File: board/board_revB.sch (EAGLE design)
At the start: 78 parts, among them Q1 ULN2003AS, Q2 ULN2003AD, Y1 8Mhz

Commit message: [Board] Fix files
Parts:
- removed IC_REF: MC1525TT, microchip:MC1525TT
- added IC_EE: 25LC040ST, microchip:25LC040ST
- added TP2: (no value), microbuilder:TESTPOINTROUND1MM
- renumbered IC_REG1 to IC_REG
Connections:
- removed net VAN: C30.1, C31.1, IC_REF.VO, STM32AN_POWER.VDDA
- new net SPI2_MISO: IC_EE.SO, STM32PORTB_H.PB14
- new net SPI2_MOSI: IC_EE.SI, STM32PORTB_H.PB15
- new net SPI2_NSS: IC_EE.!CS, STM32PORTB_H.PB12
- new net SPI2_SCK: IC_EE.SCK, STM32PORTB_H.PB13
- net +3V3: now also C30.1, C31.1, IC_EE.!WP, IC_EE.VCC, STM32AN_POWER.VDDA, TP2.P$1; no longer IC_REF.VIN
- net GND: now also IC_EE.GND; no longer IC_REF.GND
- net USB_CTRL: now also STM32PORTC_H.PC8; no longer STM32PORTB_H.PB13

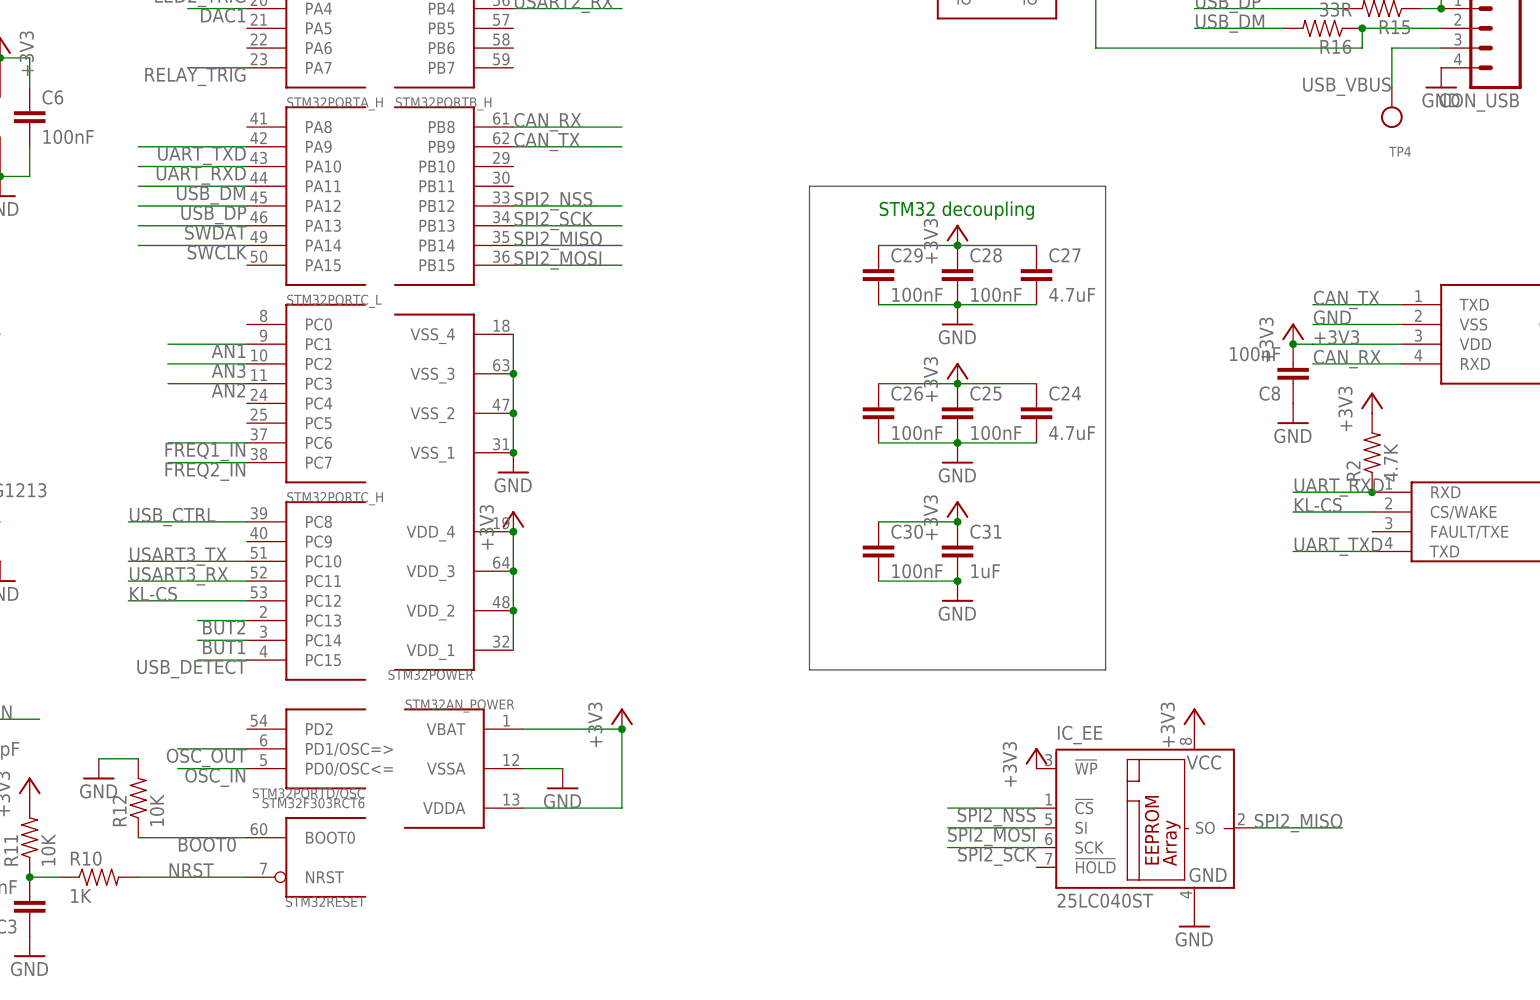
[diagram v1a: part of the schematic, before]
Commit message: [Board] Layout improvements
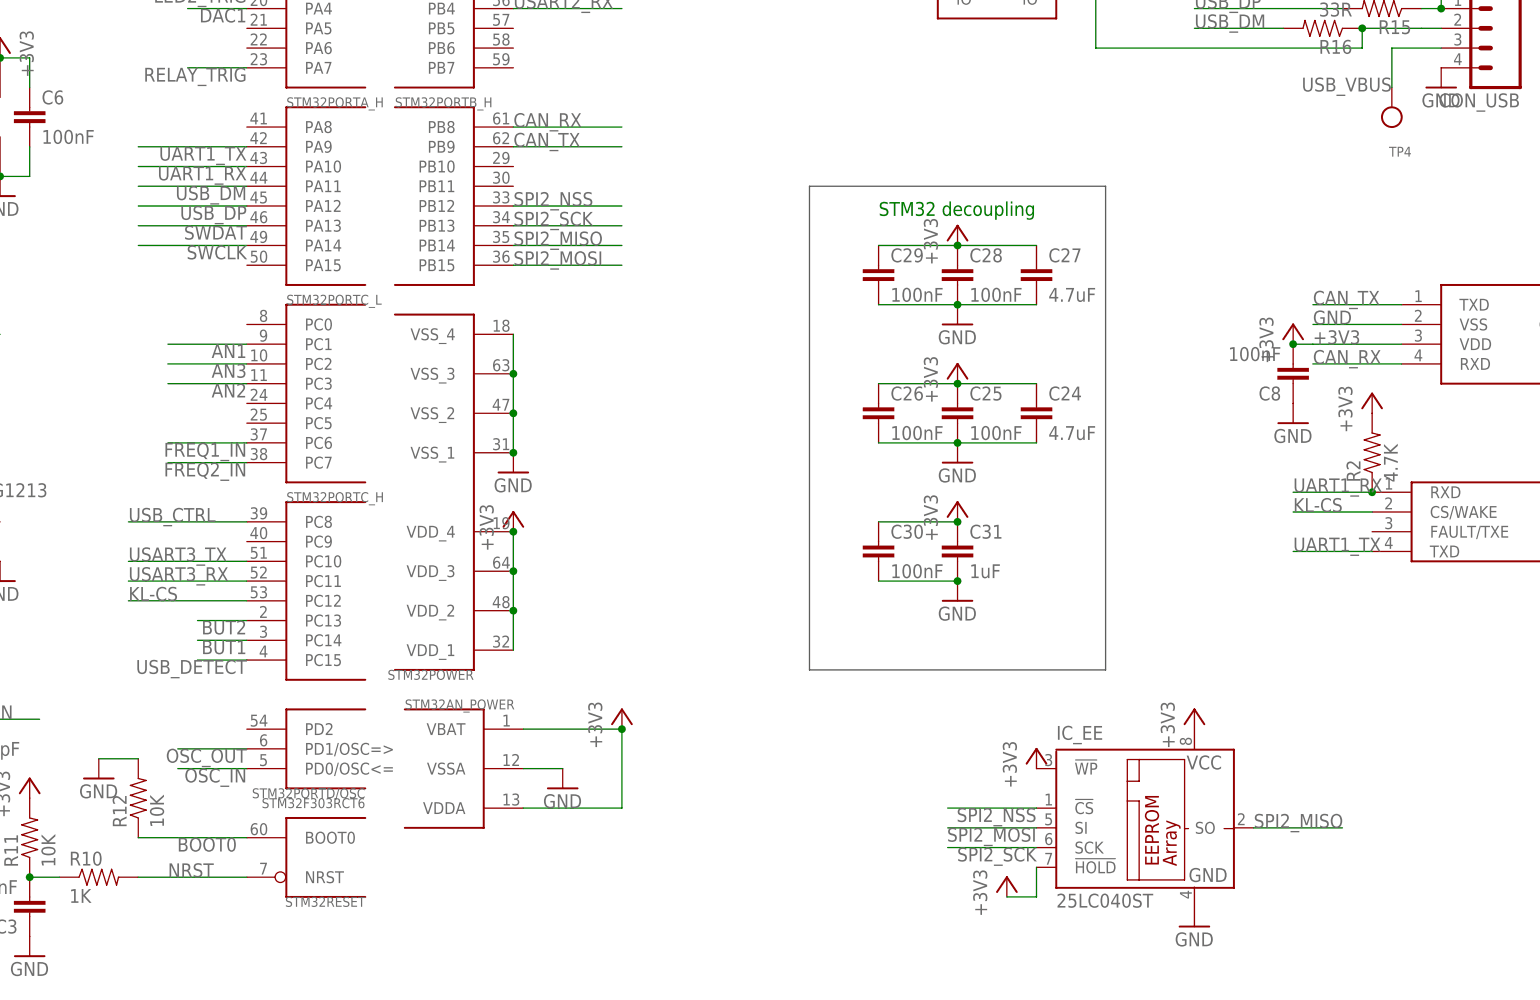
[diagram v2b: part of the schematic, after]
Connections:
- net UART_RXD renamed UART1_RX
- net UART_TXD renamed UART1_TX
- net +3V3: now also IC_EE.!HOLD
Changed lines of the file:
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@@
 <grid distance="0.05" unitdist="inch" unit="inch" style="lines" multiple="1" display="yes" altdistance="0.005" altunitdist="inch" altunit="inch"/>
 <layers>
-<layer number="1" name="Top" color="4" fill="1" visible="yes" active="no"/>
-<layer number="2" name="Route2" color="1" fill="3" visible="yes" active="no"/>
-<layer number="3" name="Route3" color="4" fill="3" visible="yes" active="no"/>
-<layer number="4" name="Route4" color="1" fill="4" visible="yes" active="no"/>
-<layer number="5" name="Route5" color="4" fill="4" visible="yes" active="no"/>
-<layer number="6" name="Route6" color="1" fill="8" visible="yes" active="no"/>
-<layer number="7" name="Route7" color="4" fill="8" visible="yes" active="no"/>
-<layer number="8" name="Route8" color="1" fill="2" visible="yes" active="no"/>
-<layer number="9" name="Route9" color="4" fill="2" visible="yes" active="no"/>
-<layer number="10" name="Route10" color="1" fill="7" visible="yes" active="no"/>
-<layer number="11" name="Route11" color="4" fill="7" visible="yes" active="no"/>
-<layer number="12" name="Route12" color="1" fill="5" visible="yes" active="no"/>
-<layer number="13" name="Route13" color="4" fill="5" visible="yes" active="no"/>
-<layer number="14" name="Route14" color="1" fill="6" visible="yes" active="no"/>
-<layer number="15" name="Route15" color="4" fill="6" visible="yes" active="no"/>
-<layer number="16" name="Bottom" color="1" fill="1" visible="yes" active="no"/>
-<layer number="17" name="Pads" color="2" fill="1" visible="yes" active="no"/>
-<layer number="18" name="Vias" color="2" fill="1" visible="yes" active="no"/>
-<layer number="19" name="Unrouted" color="6" fill="1" visible="yes" active="no"/>
-<layer number="20" name="Dimension" color="15" fill="1" visible="yes" active="no"/>
-<layer number="21" name="tPlace" color="16" fill="1" visible="yes" active="no"/>
-<layer number="22" name="bPlace" color="14" fill="1" visible="yes" active="no"/>
-<layer number="23" name="tOrigins" color="15" fill="1" visible="yes" active="no"/>
-<layer number="24" name="bOrigins" color="15" fill="1" visible="yes" active="no"/>
-<layer number="25" name="tNames" color="7" fill="1" visible="yes" active="no"/>
-<layer number="26" name="bNames" color="7" fill="1" visible="yes" active="no"/>
-<layer number="27" name="tValues" color="7" fill="1" visible="yes" active="no"/>
-<layer number="28" name="bValues" color="7" fill="1" visible="yes" active="no"/>
+<layer number="1" name="Top" color="4" fill="1" visible="no" active="no"/>
+<layer number="2" name="Route2" color="1" fill="3" visible="no" active="no"/>
+<layer number="3" name="Route3" color="4" fill="3" visible="no" active="no"/>
+<layer number="4" name="Route4" color="1" fill="4" visible="no" active="no"/>
+<layer number="5" name="Route5" color="4" fill="4" visible="no" active="no"/>
+<layer number="6" name="Route6" color="1" fill="8" visible="no" active="no"/>
+<layer number="7" name="Route7" color="4" fill="8" visible="no" active="no"/>
+<layer number="8" name="Route8" color="1" fill="2" visible="no" active="no"/>
+<layer number="9" name="Route9" color="4" fill="2" visible="no" active="no"/>
+<layer number="10" name="Route10" color="1" fill="7" visible="no" active="no"/>
+<layer number="11" name="Route11" color="4" fill="7" visible="no" active="no"/>
+<layer number="12" name="Route12" color="1" fill="5" visible="no" active="no"/>
+<layer number="13" name="Route13" color="4" fill="5" visible="no" active="no"/>
+<layer number="14" name="Route14" color="1" fill="6" visible="no" active="no"/>
+<layer number="15" name="Route15" color="4" fill="6" visible="no" active="no"/>
+<layer number="16" name="Bottom" color="1" fill="1" visible="no" active="no"/>
+<layer number="17" name="Pads" color="2" fill="1" visible="no" active="no"/>
+<layer number="18" name="Vias" color="2" fill="1" visible="no" active="no"/>
+<layer number="19" name="Unrouted" color="6" fill="1" visible="no" active="no"/>
+<layer number="20" name="Dimension" color="15" fill="1" visible="no" active="no"/>
+<layer number="21" name="tPlace" color="16" fill="1" visible="no" active="no"/>
+<layer number="22" name="bPlace" color="14" fill="1" visible="no" active="no"/>
+<layer number="23" name="tOrigins" color="15" fill="1" visible="no" active="no"/>
+<layer number="24" name="bOrigins" color="15" fill="1" visible="no" active="no"/>
+<layer number="25" name="tNames" color="7" fill="1" visible="no" active="no"/>
+<layer number="26" name="bNames" color="7" fill="1" visible="no" active="no"/>
+<layer number="27" name="tValues" color="7" fill="1" visible="no" active="no"/>
+<layer number="28" name="bValues" color="7" fill="1" visible="no" active="no"/>
 <layer number="29" name="tStop" color="7" fill="3" visible="no" active="no"/>
 <layer number="30" name="bStop" color="7" fill="6" visible="no" active="no"/>
@@
 <layer number="35" name="tGlue" color="7" fill="4" visible="no" active="no"/>
 <layer number="36" name="bGlue" color="7" fill="5" visible="no" active="no"/>
-<layer number="37" name="tTest" color="7" fill="1" visible="yes" active="no"/>
-<layer number="38" name="bTest" color="7" fill="1" visible="yes" active="no"/>
+<layer number="37" name="tTest" color="7" fill="1" visible="no" active="no"/>
+<layer number="38" name="bTest" color="7" fill="1" visible="no" active="no"/>
 <layer number="39" name="tKeepout" color="4" fill="11" visible="no" active="no"/>
 <layer number="40" name="bKeepout" color="1" fill="11" visible="no" active="no"/>
@@
 <layer number="44" name="Drills" color="7" fill="1" visible="no" active="no"/>
 <layer number="45" name="Holes" color="7" fill="1" visible="no" active="no"/>
-<layer number="46" name="Milling" color="3" fill="1" visible="yes" active="no"/>
-<layer number="47" name="Measures" color="7" fill="1" visible="yes" active="no"/>
-<layer number="48" name="Document" color="7" fill="1" visible="yes" active="no"/>
-<layer number="49" name="Reference" color="7" fill="1" visible="yes" active="no"/>
-<layer number="50" name="dxf" color="7" fill="1" visible="yes" active="no"/>
-<layer number="51" name="tDocu" color="6" fill="1" visible="yes" active="no"/>
-<layer number="52" name="bDocu" color="7" fill="1" visible="yes" active="no"/>
-<layer number="53" name="tGND_GNDA" color="7" fill="9" visible="yes" active="no"/>
-<layer number="54" name="bGND_GNDA" color="1" fill="9" visible="yes" active="no"/>
-<layer number="56" name="wert" color="7" fill="1" visible="yes" active="no"/>
-<layer number="57" name="tCAD" color="7" fill="1" visible="yes" active="no"/>
+<layer number="46" name="Milling" color="3" fill="1" visible="no" active="no"/>
+<layer number="47" name="Measures" color="7" fill="1" visible="no" active="no"/>
+<layer number="48" name="Document" color="7" fill="1" visible="no" active="no"/>
+<layer number="49" name="Reference" color="7" fill="1" visible="no" active="no"/>
+<layer number="50" name="dxf" color="7" fill="1" visible="no" active="no"/>
+<layer number="51" name="tDocu" color="6" fill="1" visible="no" active="no"/>
+<layer number="52" name="bDocu" color="7" fill="1" visible="no" active="no"/>
+<layer number="53" name="tGND_GNDA" color="7" fill="9" visible="no" active="no"/>
+<layer number="54" name="bGND_GNDA" color="1" fill="9" visible="no" active="no"/>
+<layer number="56" name="wert" color="7" fill="1" visible="no" active="no"/>
+<layer number="57" name="tCAD" color="7" fill="1" visible="no" active="no"/>
 <layer number="91" name="Nets" color="2" fill="1" visible="yes" active="yes"/>
 <layer number="92" name="Busses" color="1" fill="1" visible="yes" active="yes"/>
@@
 <part name="IC_EE" library="microchip" deviceset="25*" device="ST" technology="LC040"/>
 <part name="+3V16" library="supply1" deviceset="+3V3" device=""/>
+<part name="+3V18" library="supply1" deviceset="+3V3" device=""/>
 </parts>
 <sheets>
@@
 <instance part="IC_EE" gate="G$1" x="256.54" y="22.86"/>
 <instance part="+3V16" gate="G$1" x="243.84" y="33.02"/>
+<instance part="+3V18" gate="G$1" x="240.03" y="16.51"/>
 </instances>
 <busses>
@@
 <pinref part="+3V16" gate="G$1" pin="+3V3"/>
 </segment>
+<segment>
+<pinref part="+3V18" gate="G$1" pin="+3V3"/>
+<pinref part="IC_EE" gate="G$1" pin="!HOLD"/>
+<wire x1="240.03" y1="13.97" x2="243.84" y2="13.97" width="0.1524" layer="91"/>
+<wire x1="243.84" y1="13.97" x2="243.84" y2="17.78" width="0.1524" layer="91"/>
+</segment>
 </net>
 <net name="+12V" class="0">
@@
 </segment>
 </net>
-<net name="UART_RXD" class="0">
+<net name="UART1_RX" class="0">
 <segment>
 <wire x1="287.02" y1="66.04" x2="276.86" y2="66.04" width="0.1524" layer="91"/>
@@
 </segment>
 </net>
-<net name="UART_TXD" class="0">
+<net name="UART1_TX" class="0">
 <segment>
 <wire x1="287.02" y1="58.42" x2="276.86" y2="58.42" width="0.1524" layer="91"/>
